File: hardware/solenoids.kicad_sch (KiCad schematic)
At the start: 62 parts

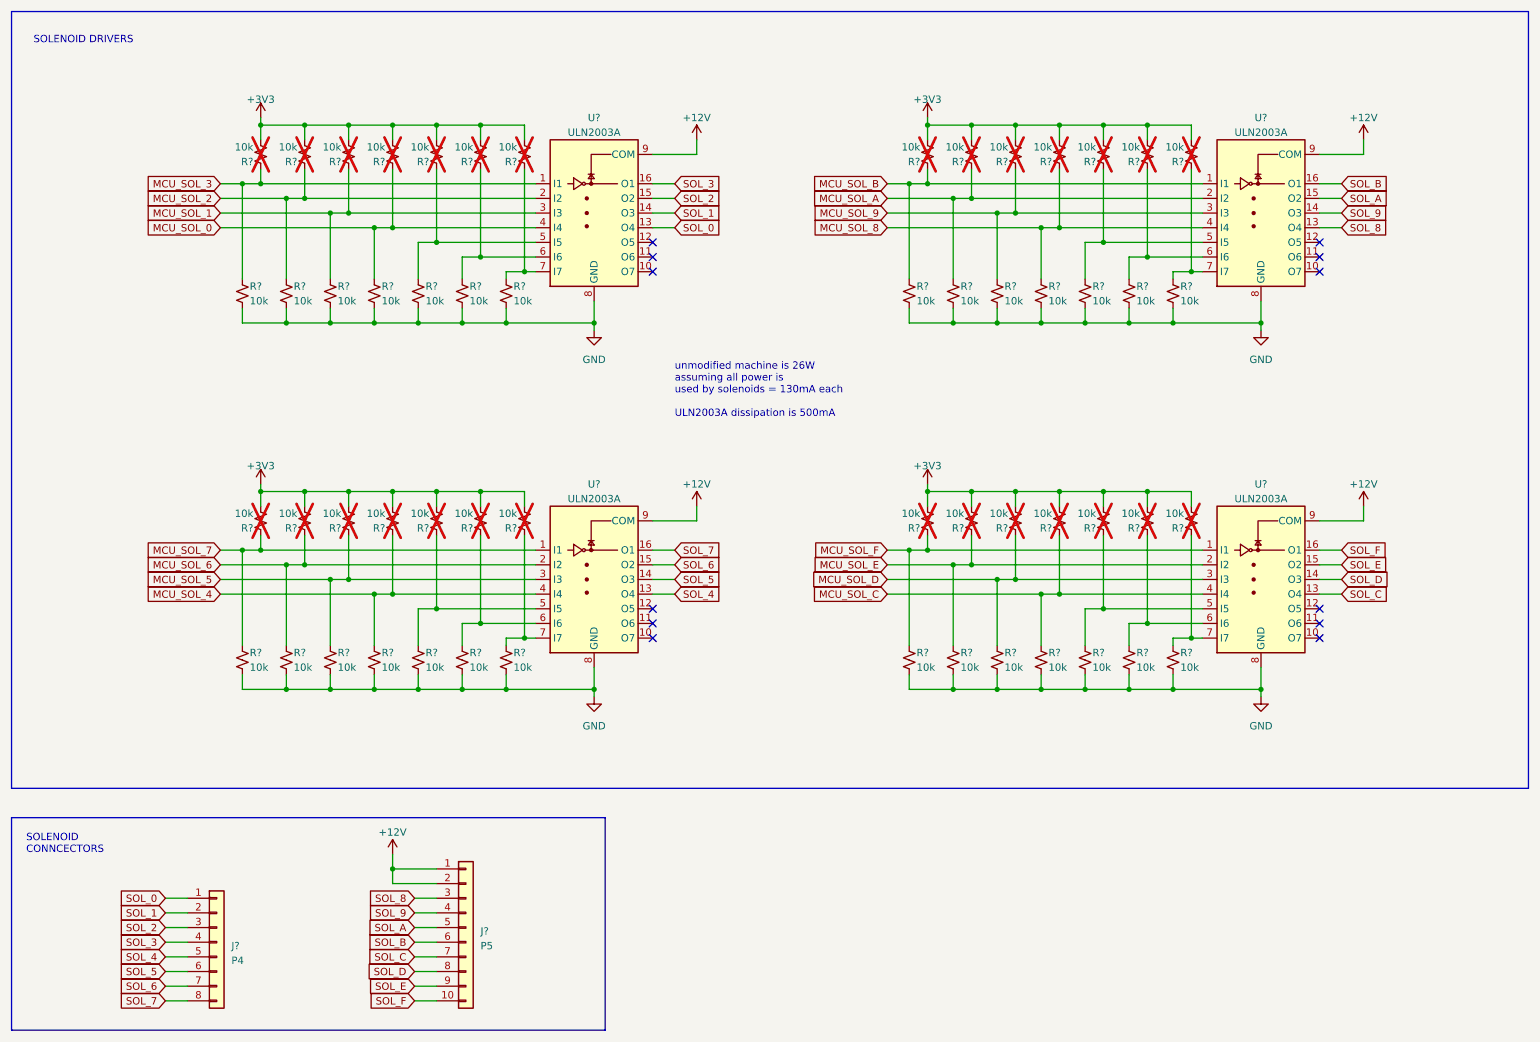
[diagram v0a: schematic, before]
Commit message: work on firmware and swap solenoid banks to match actual pinout
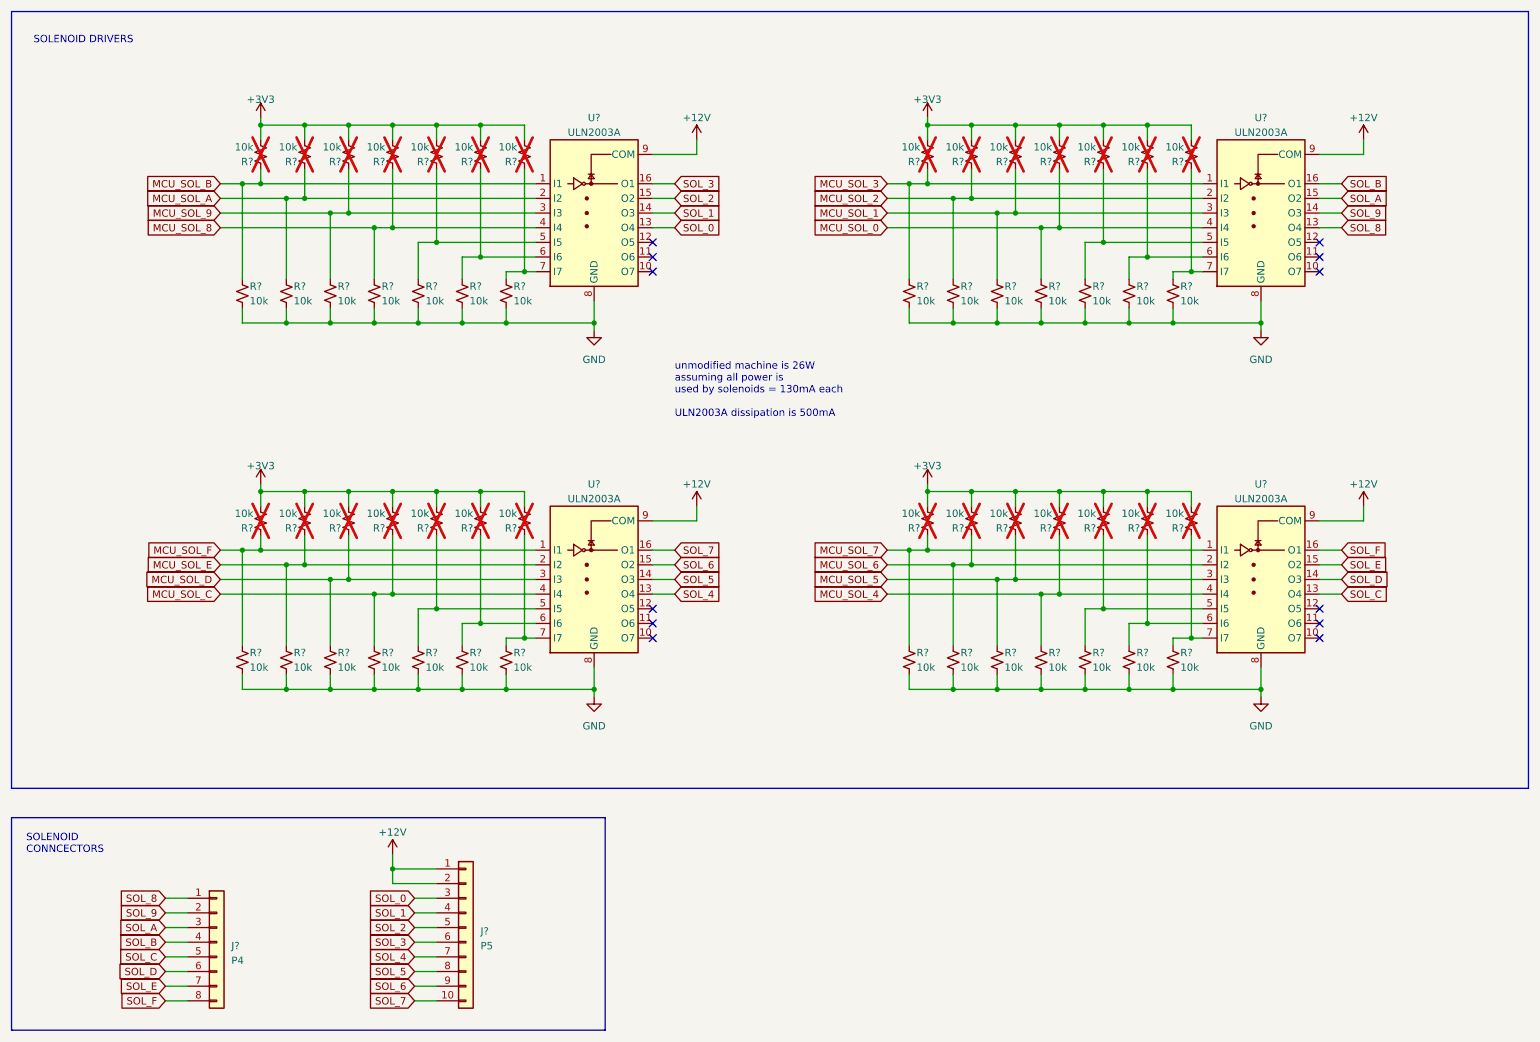
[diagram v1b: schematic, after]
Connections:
- net MCU_SOL_0: now also R?.1, R?.1, U?.4 (I4); no longer R?.1, R?.1, U?.4 (I4)
- net MCU_SOL_1: now also R?.1, R?.1, U?.3 (I3); no longer R?.1, R?.1, U?.3 (I3)
- net MCU_SOL_2: now also R?.1, R?.1, U?.2 (I2); no longer R?.1, R?.1, U?.2 (I2)
- net MCU_SOL_3: now also R?.1, R?.1, U?.1 (I1); no longer R?.1, R?.1, U?.1 (I1)
- net MCU_SOL_4: now also R?.1, R?.1, U?.4 (I4); no longer R?.1, R?.1, U?.4 (I4)
- net MCU_SOL_5: now also R?.1, R?.1, U?.3 (I3); no longer R?.1, R?.1, U?.3 (I3)
- net MCU_SOL_6: now also R?.1, R?.1, U?.2 (I2); no longer R?.1, R?.1, U?.2 (I2)
- net MCU_SOL_7: now also R?.1, R?.1, U?.1 (I1); no longer R?.1, R?.1, U?.1 (I1)
- net MCU_SOL_8: now also R?.1, R?.1, U?.4 (I4); no longer R?.1, R?.1, U?.4 (I4)
- net MCU_SOL_9: now also R?.1, R?.1, U?.3 (I3); no longer R?.1, R?.1, U?.3 (I3)
- net MCU_SOL_A: now also R?.1, R?.1, U?.2 (I2); no longer R?.1, R?.1, U?.2 (I2)
- net MCU_SOL_B: now also R?.1, R?.1, U?.1 (I1); no longer R?.1, R?.1, U?.1 (I1)
- net MCU_SOL_C: now also R?.1, R?.1, U?.4 (I4); no longer R?.1, R?.1, U?.4 (I4)
- net MCU_SOL_D: now also R?.1, R?.1, U?.3 (I3); no longer R?.1, R?.1, U?.3 (I3)
- net MCU_SOL_E: now also R?.1, R?.1, U?.2 (I2); no longer R?.1, R?.1, U?.2 (I2)
- net MCU_SOL_F: now also R?.1, R?.1, U?.1 (I1); no longer R?.1, R?.1, U?.1 (I1)
- net SOL_0: now also J?.3 (Pin_3); no longer J?.1 (Pin_1)
- net SOL_1: now also J?.4 (Pin_4); no longer J?.2 (Pin_2)
- net SOL_2: now also J?.5 (Pin_5); no longer J?.3 (Pin_3)
- net SOL_3: now also J?.6 (Pin_6); no longer J?.4 (Pin_4)
- net SOL_4: now also J?.7 (Pin_7); no longer J?.5 (Pin_5)
- net SOL_5: now also J?.8 (Pin_8); no longer J?.6 (Pin_6)
- net SOL_6: now also J?.9 (Pin_9); no longer J?.7 (Pin_7)
- net SOL_7: now also J?.10 (Pin_10); no longer J?.8 (Pin_8)
- net SOL_8: now also J?.1 (Pin_1); no longer J?.3 (Pin_3)
- net SOL_9: now also J?.2 (Pin_2); no longer J?.4 (Pin_4)
- net SOL_A: now also J?.3 (Pin_3); no longer J?.5 (Pin_5)
- net SOL_B: now also J?.4 (Pin_4); no longer J?.6 (Pin_6)
- net SOL_C: now also J?.5 (Pin_5); no longer J?.7 (Pin_7)
- net SOL_D: now also J?.6 (Pin_6); no longer J?.8 (Pin_8)
- net SOL_E: now also J?.7 (Pin_7); no longer J?.9 (Pin_9)
- net SOL_F: now also J?.8 (Pin_8); no longer J?.10 (Pin_10)
